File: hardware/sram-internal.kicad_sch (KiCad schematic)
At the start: 3 parts, among them U12 IS66WV51216EBLL-55TLI

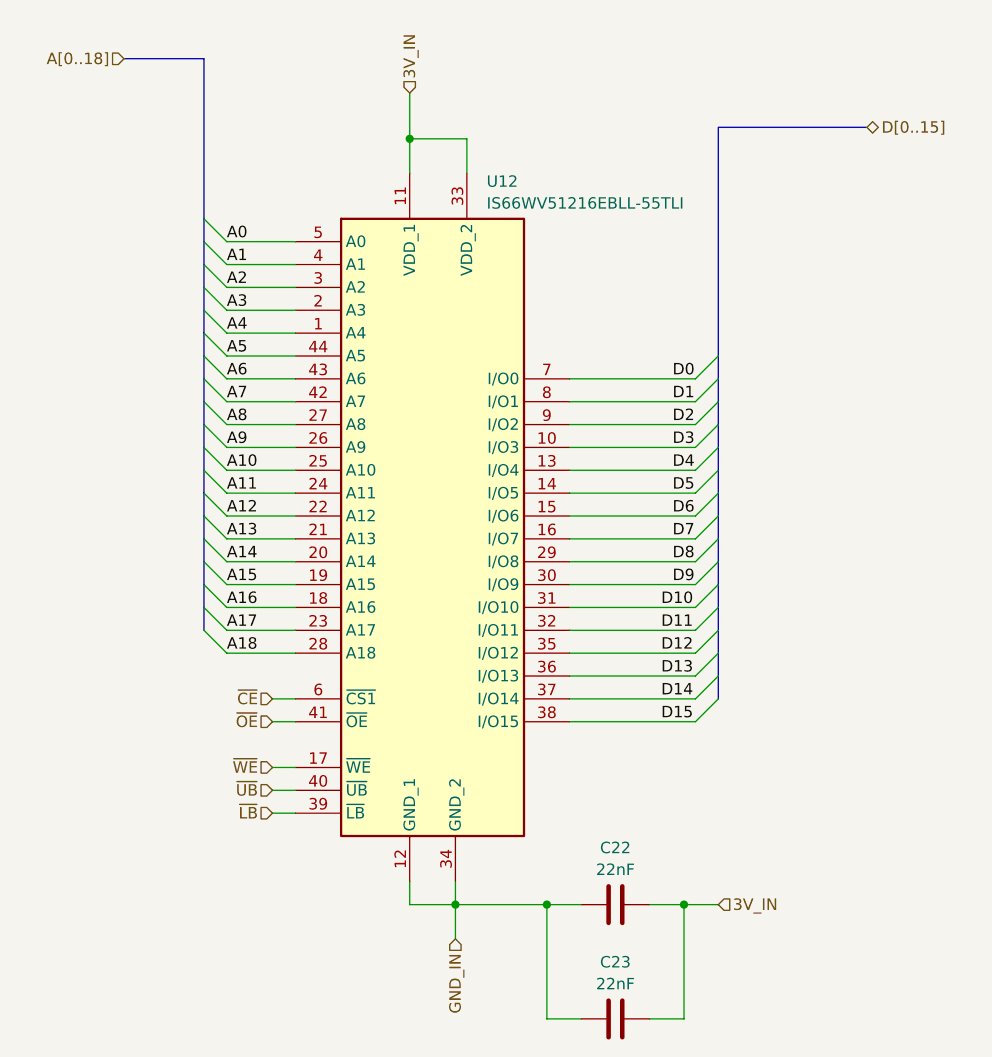
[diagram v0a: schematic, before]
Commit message: Massively reorganize board designs
Now planning to have most assembly done by JLCPCB, so trace sizes,
part selections, etc. are set accordingly.

New boards are:
 - cartridge interface & flash
 - microcontroller & registers
 - sram x2
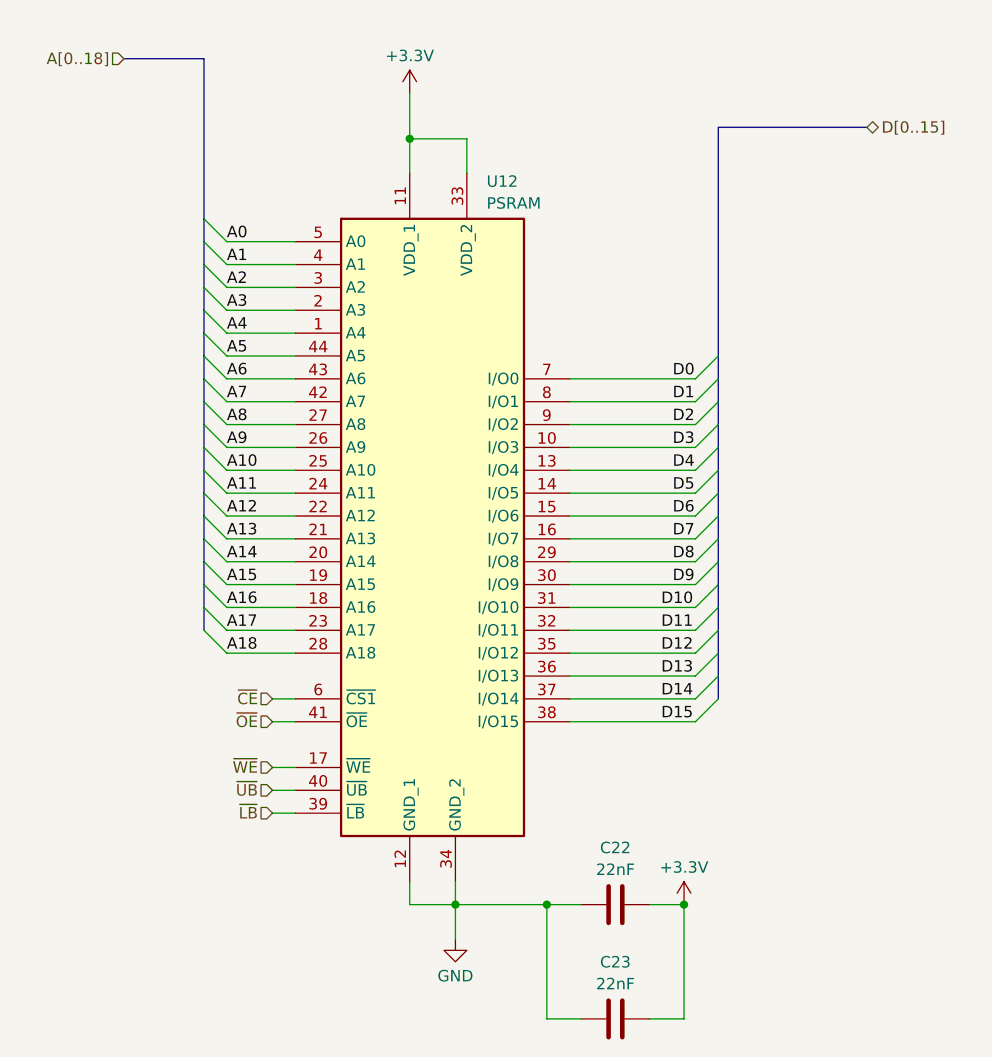
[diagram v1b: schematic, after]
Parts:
- C22, C23: footprint Capacitor_SMD:C_1206_3216Metric -> Capacitor_SMD:C_0603_1608Metric; JLCPCB Part Number (none) -> CL10B223KB8NNNC; Mouser Part Number (none) -> 80-C0603C223K4R; Part Number (none) -> C0603C223K4RACTU
- U12: value IS66WV51216EBLL-55TLI -> PSRAM; Height 1.2 -> (none); JLCPCB Part Number (none) -> C1348810; Manufacturer_Name Integrated Silicon Solution Inc. -> (none); Manufacturer_Part_Number IS66WV51216EBLL-55TLI -> (none); Mouser Price/Stock https://www.mouser.com/Search/Refine.aspx?Keyword=870-66WV5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 -> (none); Part Number (none) -> IS66WV51216EBLL-55TLI
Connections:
- net 3V_IN renamed +3.3V
- net GND_IN renamed GND

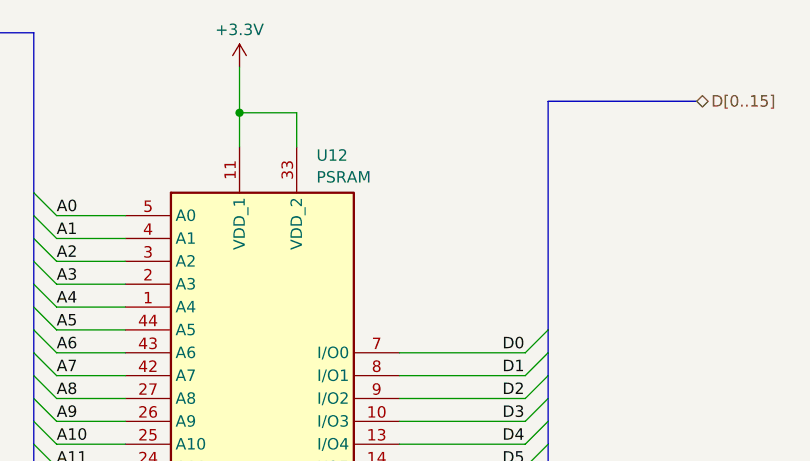
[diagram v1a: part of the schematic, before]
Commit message: Redesign SRAM address decoders
 - Redo original address decoder for SRAM_CE signal
 - Replace NAND gate with another address decoder
   - Simplifies the BOM by removing a one-off part
   - Stabilizes the control signals by making sure SEGA_CONTROL and
     UC_CONTROL can never be active at once (one does not depend on
     the other)
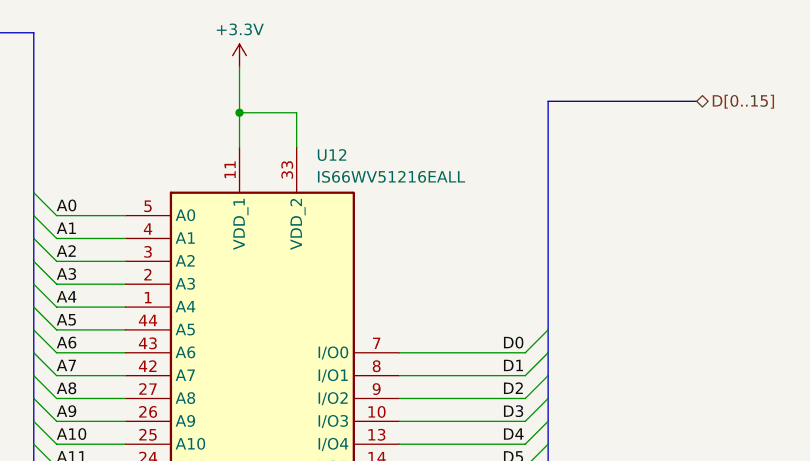
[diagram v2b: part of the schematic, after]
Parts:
- U12: value PSRAM -> IS66WV51216EALL
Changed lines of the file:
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@@
 			)
 		)
-		(property "Value" "PSRAM"
+		(property "Value" "IS66WV51216EALL"
 			(at 112.6841 46.5398 0)
 			(effects

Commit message: Fix SRAM CE signaling
It turns out that a PSRAM's ~{CE} signal may not stay on at all times.
There is a maximum pulse width of 15us for this chipset, so that the
DRAM internal to the PSRAM can go through a refresh cycle.

Tying ~{CE} to ~{WE} (for writes) or ~{SEGA_CE} (for reads) seems to
meet all the timing requirements.  This has yet to be verified,
though, for a lack of test pads for all ~{CE} signals on the previous
board revision.

(PCB routing in progress, will commit later.)
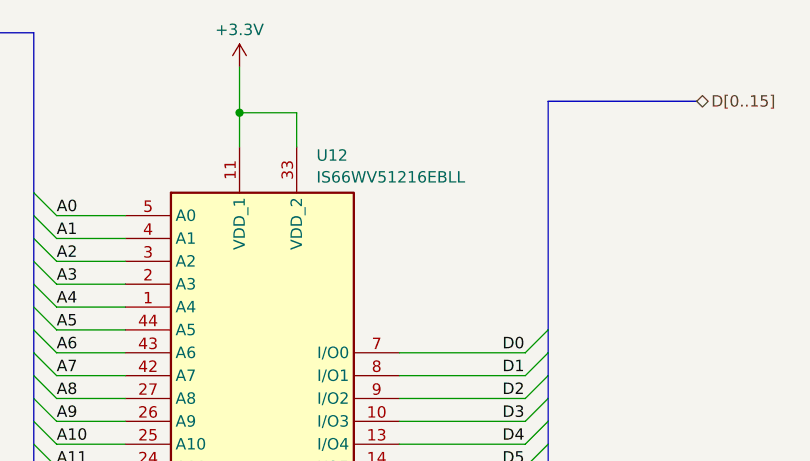
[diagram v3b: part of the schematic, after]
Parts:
- U12: value IS66WV51216EALL -> IS66WV51216EBLL
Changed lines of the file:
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@@
 			)
 		)
-		(property "Value" "IS66WV51216EALL"
+		(property "Value" "IS66WV51216EBLL"
 			(at 112.6841 46.5398 0)
 			(effects

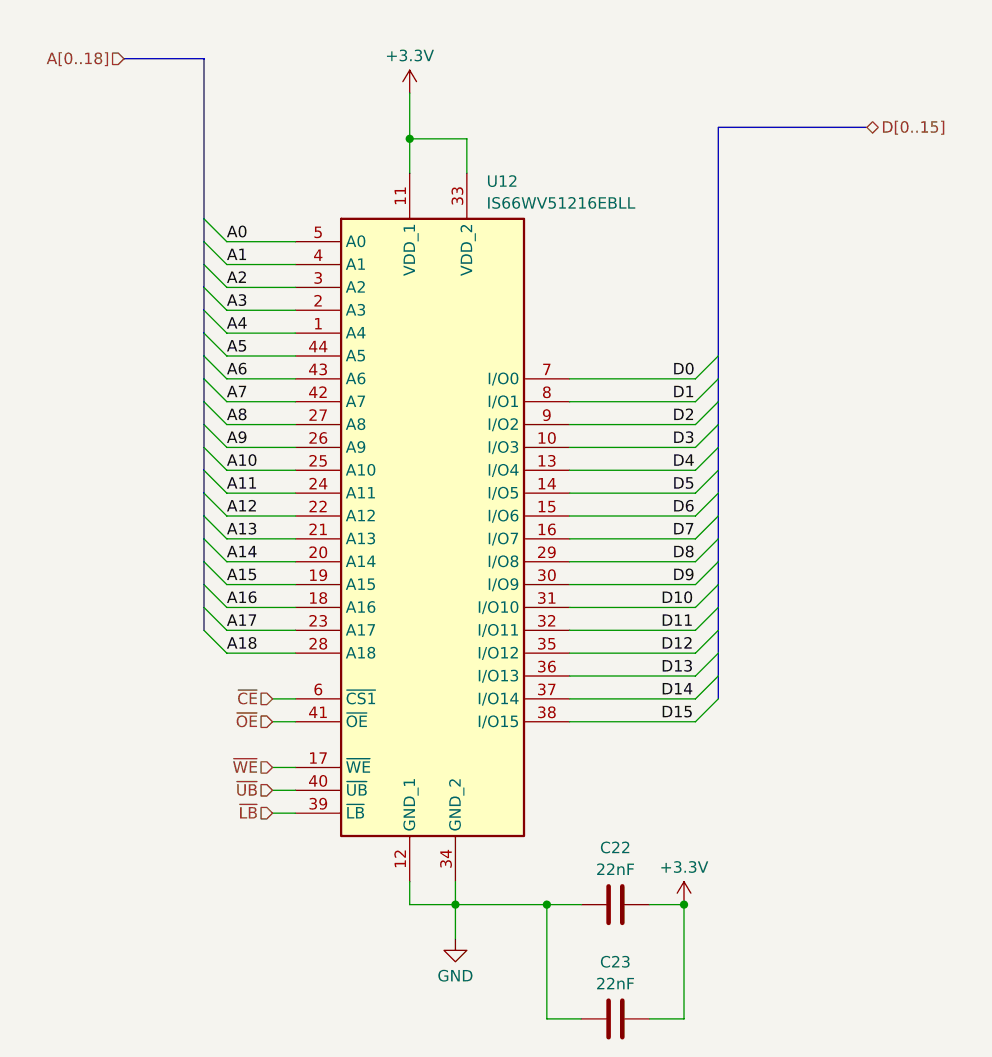
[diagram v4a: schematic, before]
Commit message: Move SRAM bank board design into shareable subsheet
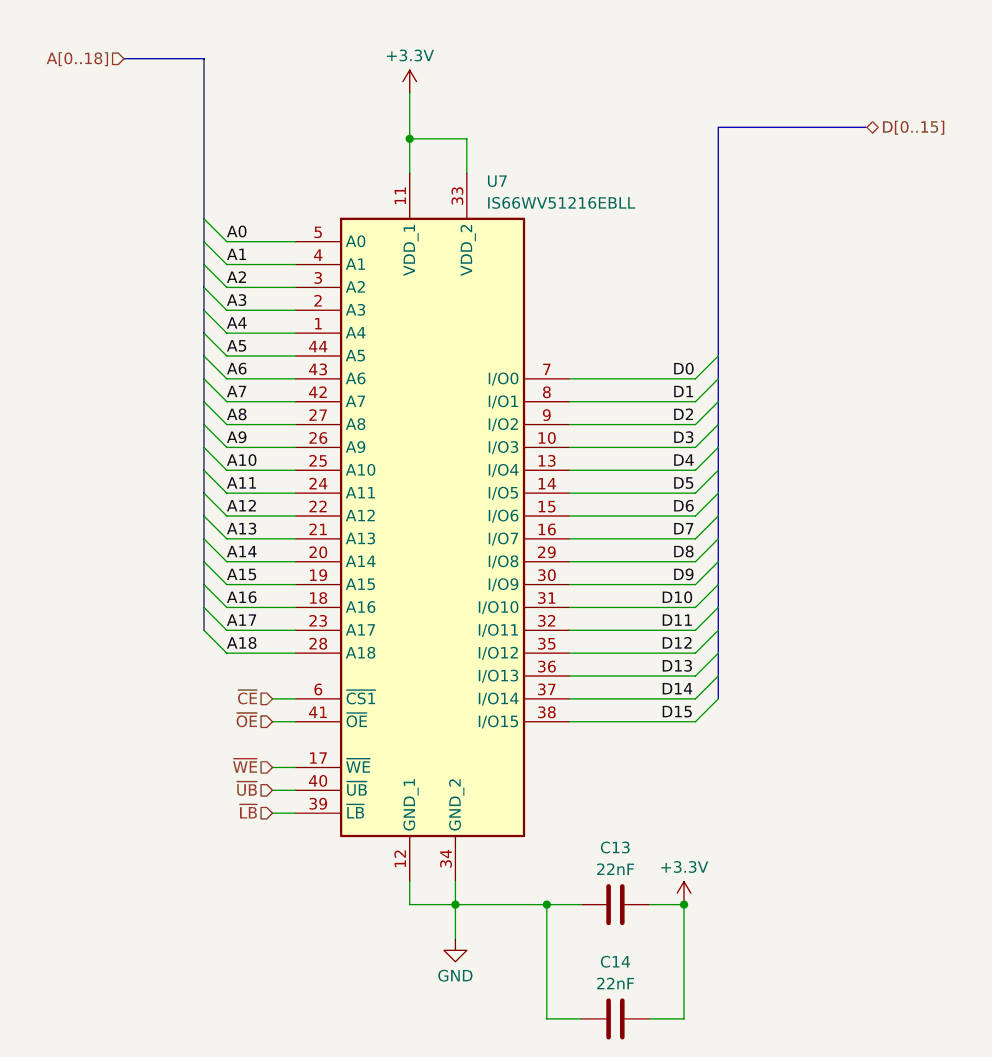
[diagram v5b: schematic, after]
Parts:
- renumbered C22 to C13, C23 to C14, U12 to U7
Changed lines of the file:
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@@
 		(dnp no)
 		(fields_autoplaced yes)
-		(property "Reference" "#PWR023"
+		(property "Reference" "#PWR024"
 			(at 109.22 134.62 0)
 			(effects
@@
 		)
 		(instances
-			(project ""
-				(path "/620c762c-1ae9-4ea9-ab1a-d023a8da85ac/498fb6bd-8d43-4ac2-b67e-254cc3671223"
-					(reference "#PWR023")
+			(project "sram-bank"
+				(path "/620c762c-1ae9-4ea9-ab1a-d023a8da85ac/de6964c0-b8e7-4813-9bb5-2e4faf4431cb/3d478650-c721-4e59-90b6-3e9b8fac63c3"
+					(reference "#PWR024")
 					(unit 1)
 				)
@@
 		(dnp no)
 		(fields_autoplaced yes)
-		(property "Reference" "C22"
+		(property "Reference" "C13"
 			(at 127 118.1565 90)
 			(effects
@@
 		(instances
 			(project "sram-bank"
-				(path "/620c762c-1ae9-4ea9-ab1a-d023a8da85ac/498fb6bd-8d43-4ac2-b67e-254cc3671223"
-					(reference "C22")
+				(path "/620c762c-1ae9-4ea9-ab1a-d023a8da85ac/de6964c0-b8e7-4813-9bb5-2e4faf4431cb/3d478650-c721-4e59-90b6-3e9b8fac63c3"
+					(reference "C13")
 					(unit 1)
 				)
@@
 		(dnp no)
 		(fields_autoplaced yes)
-		(property "Reference" "C23"
+		(property "Reference" "C14"
 			(at 127 130.8565 90)
 			(effects
@@
 		(instances
 			(project "sram-bank"
-				(path "/620c762c-1ae9-4ea9-ab1a-d023a8da85ac/498fb6bd-8d43-4ac2-b67e-254cc3671223"
-					(reference "C23")
+				(path "/620c762c-1ae9-4ea9-ab1a-d023a8da85ac/de6964c0-b8e7-4813-9bb5-2e4faf4431cb/3d478650-c721-4e59-90b6-3e9b8fac63c3"
+					(reference "C14")
 					(unit 1)
 				)
@@
 		(dnp no)
 		(fields_autoplaced yes)
-		(property "Reference" "#PWR022"
+		(property "Reference" "#PWR025"
 			(at 134.62 128.27 0)
 			(effects
@@
 		(instances
 			(project "sram-bank"
-				(path "/620c762c-1ae9-4ea9-ab1a-d023a8da85ac/498fb6bd-8d43-4ac2-b67e-254cc3671223"
-					(reference "#PWR022")
+				(path "/620c762c-1ae9-4ea9-ab1a-d023a8da85ac/de6964c0-b8e7-4813-9bb5-2e4faf4431cb/3d478650-c721-4e59-90b6-3e9b8fac63c3"
+					(reference "#PWR025")
 					(unit 1)
 				)
@@
 		(dnp no)
 		(fields_autoplaced yes)
-		(property "Reference" "#PWR021"
+		(property "Reference" "#PWR023"
 			(at 104.14 38.1 0)
 			(effects
@@
 		(instances
 			(project "sram-bank"
-				(path "/620c762c-1ae9-4ea9-ab1a-d023a8da85ac/498fb6bd-8d43-4ac2-b67e-254cc3671223"
-					(reference "#PWR021")
+				(path "/620c762c-1ae9-4ea9-ab1a-d023a8da85ac/de6964c0-b8e7-4813-9bb5-2e4faf4431cb/3d478650-c721-4e59-90b6-3e9b8fac63c3"
+					(reference "#PWR023")
 					(unit 1)
 				)
@@
 		(dnp no)
 		(fields_autoplaced yes)
-		(property "Reference" "U12"
+		(property "Reference" "U7"
 			(at 112.6841 44.1155 0)
 			(effects
@@
 		(instances
 			(project "sram-bank"
-				(path "/620c762c-1ae9-4ea9-ab1a-d023a8da85ac/498fb6bd-8d43-4ac2-b67e-254cc3671223"
-					(reference "U12")
+				(path "/620c762c-1ae9-4ea9-ab1a-d023a8da85ac/de6964c0-b8e7-4813-9bb5-2e4faf4431cb/3d478650-c721-4e59-90b6-3e9b8fac63c3"
+					(reference "U7")
 					(unit 1)
 				)
